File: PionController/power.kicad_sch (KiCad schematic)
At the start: 25 parts, among them U2 TPS562200, U3 TPS562200

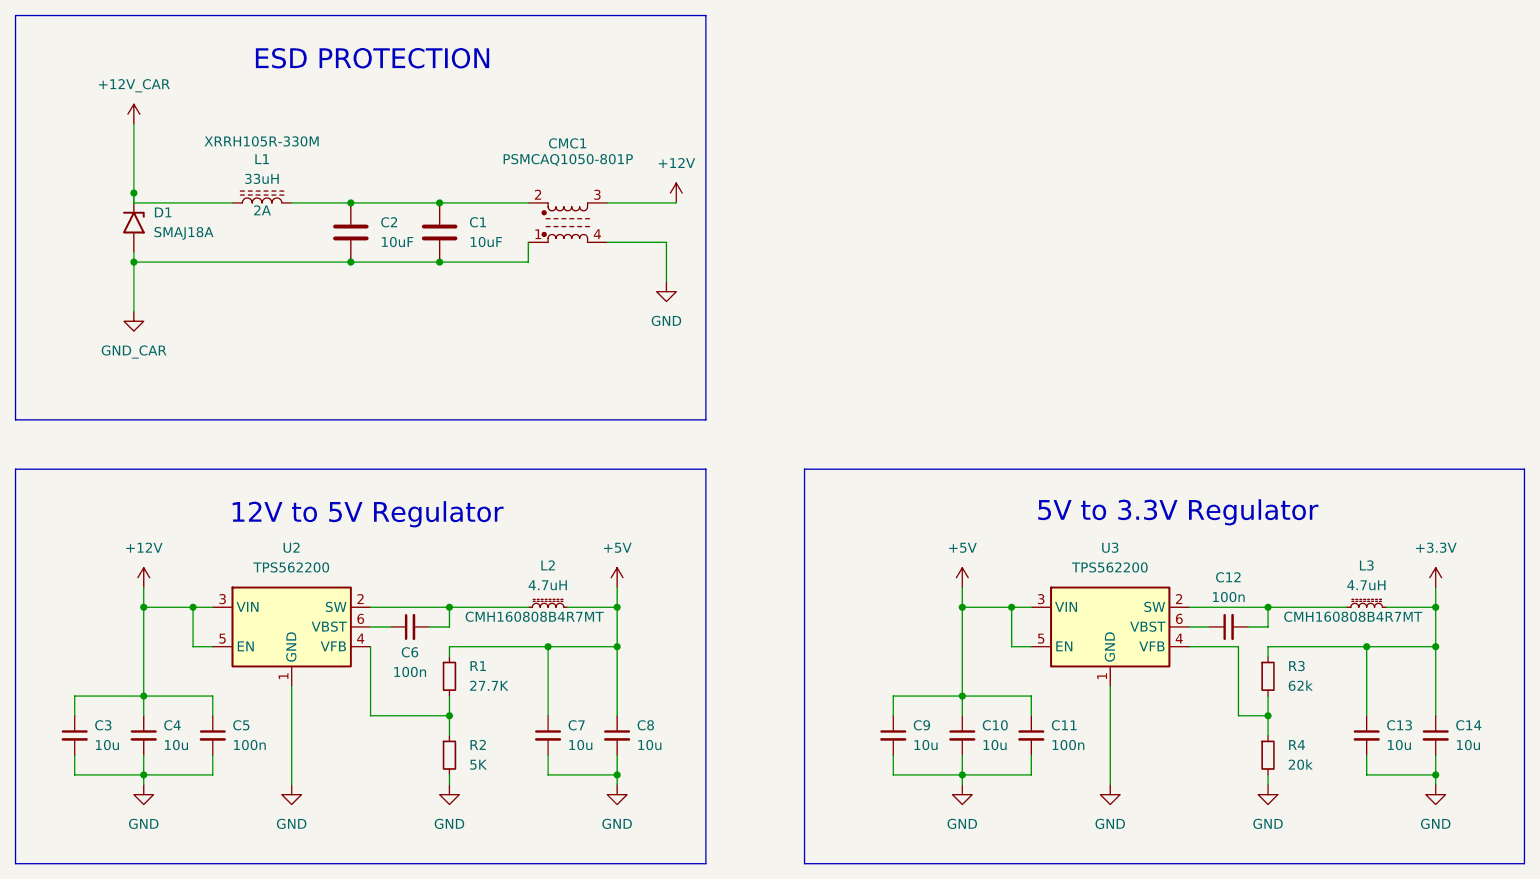
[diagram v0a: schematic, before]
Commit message: Fixing Ivan's remarks and adding the forgotten pull-down resistor
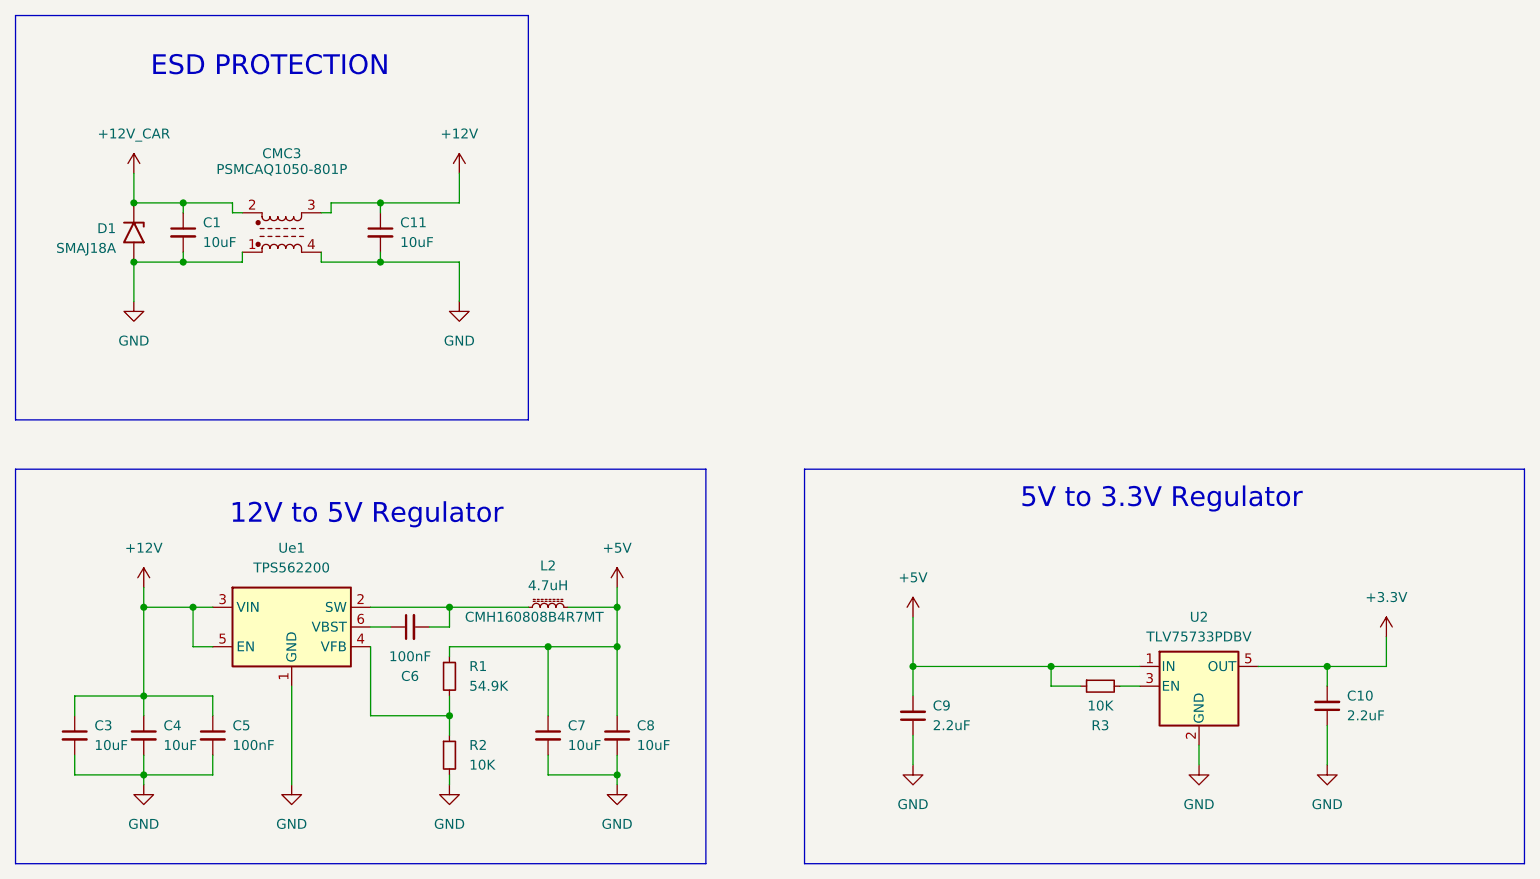
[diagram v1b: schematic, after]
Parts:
- removed C1, C2: 10uF, Capacitor_SMD:C_1210_3225Metric, symbol Device:C
- removed C12: 100n, Capacitor_SMD:C_0603_1608Metric, symbol Device:C_Small
- removed C13, C14: 10u, Capacitor_SMD:C_0603_1608Metric, symbol Device:C_Small
- removed L1: 33uH, Inductor_SMD:L_TDK_SLF10145, symbol Device:L_Ferrite
- removed L3: 4.7uH, Inductor_SMD:L_0603_1608Metric, symbol Device:L_Ferrite_Small
- removed R4: 20k, Resistor_SMD:R_0402_1005Metric, symbol Device:R_Small
- removed U3: TPS562200, Package_TO_SOT_SMD:SOT-23-6, symbol Regulator_Switching:TPS562200
- added C1: 10uF, Capacitor_SMD:C_1210_3225Metric, symbol Device:C_Small
- added U2: TLV75733PDBV, Package_TO_SOT_SMD:SOT-23-5, symbol Regulator_Linear:TLV75733PDBV
- C10, C9: value 10u -> 2.2uF; LCSC C7472961 -> C914769; MPN HGC0603R5106M250NTHJ -> (none); Manufacturer (none) -> CC0603KRX7R7BB225
- C11: value 100n -> 10uF; footprint Capacitor_SMD:C_0603_1608Metric -> Capacitor_SMD:C_1210_3225Metric; LCSC C6119861 -> C596319; MPN CGA0603X7R104K250JT -> (none); Manufacturer (none) -> CC1210KKX7R9BB106
- C3, C4, C7, C8: value 10u -> 10uF; footprint Capacitor_SMD:C_0603_1608Metric -> Capacitor_SMD:C_1210_3225Metric; LCSC C7472961 -> C596319; Manufacturer HGC0603R5106M250NTHJ -> CC1210KKX7R9BB106
- C5, C6: value 100n -> 100nF; footprint Capacitor_SMD:C_0603_1608Metric -> Capacitor_SMD:C_0805_2012Metric; LCSC C6119861 -> C111492; Manufacturer CGA0603X7R104K250JT -> CC0805JRX7R9BB104
- D1: LCSC (none) -> C148219; Manufacturer (none) -> SMAJ18A
- R1: value 27.7K -> 54.9K; footprint (none) -> Resistor_SMD:R_0805_2012Metric; LCSC C863005 -> C865555; Manufacturer RT0603DRE0727K7L -> RT0805BRD0754K9L
- R2: value 5K -> 10K; footprint (none) -> Resistor_SMD:R_0805_2012Metric; LCSC C870818 -> C110775; Manufacturer RT1206BRD075KL -> RT0805BRD0710KL
- R3: value 62k -> 10K; footprint Resistor_SMD:R_0402_1005Metric -> Resistor_SMD:R_0805_2012Metric; LCSC C37825 -> C84376; MPN 0402WGF6202TCE -> (none); Manufacturer (none) -> RC0805FR-0710KL
- renumbered CMC1 to CMC3, U2 to Ue1
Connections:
- net GND_CAR is gone; now on net GND: CMC3.1, D1.2 (A2)
- net +12V: now also C11.1
- net +12V_CAR: now also CMC3.2, C1.1
- net +3.3V: now also C10.2, U2.5 (OUT); no longer R3.1
- net +5V: now also C9.2, R3.1, U2.1 (IN); no longer C10.1, C11.1, C9.1
- net GND: now also C10.1, C9.1, C1.2, U2.2 (GND); no longer C10.2, C9.2
- net at R3.2: now also U2.3 (EN)
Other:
- moved on the sheet: CMC3, D1

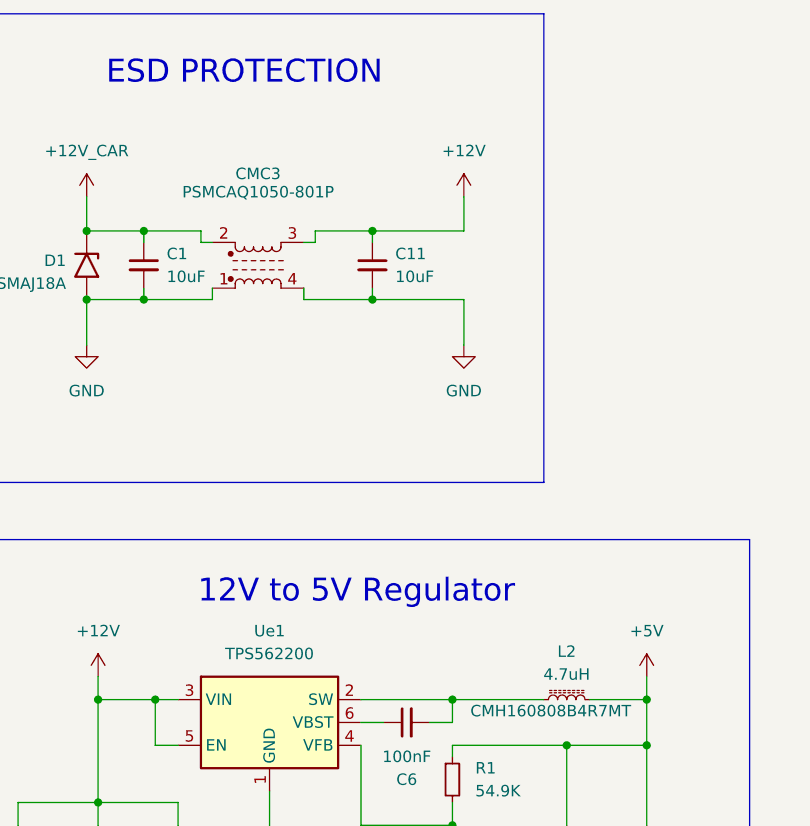
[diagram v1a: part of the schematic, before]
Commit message: Fixed reference designators in SCH and moved PCB silkscreen positions for better visibility
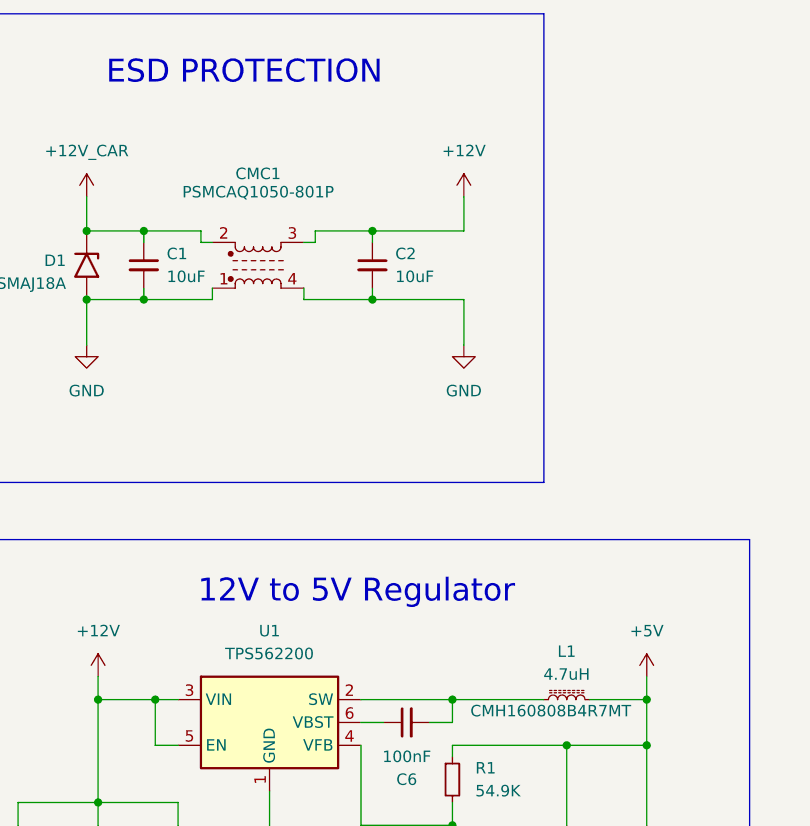
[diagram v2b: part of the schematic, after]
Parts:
- R3: Manufacturer RC0805FR-0710KL -> RC0805FR-0710KL
- renumbered C11 to C2, CMC3 to CMC1, L2 to L1, Ue1 to U1
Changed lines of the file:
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@@
+			)
+		)
+		(property "Package/Footprint" ""
+			(at 137.16 107.95 0)
+			(effects
+				(font
+					(size 1.27 1.27)
+				)
+				(hide yes)
 			)
 		)
@@
 			)
 		)
+		(property "Package/Footprint" ""
+			(at 43.18 45.72 0)
+			(effects
+				(font
+					(size 1.27 1.27)
+				)
+				(hide yes)
+			)
+		)
 		(pin "1"
 		)
@@
 			)
 		)
+		(property "Package/Footprint" ""
+			(at 77.47 102.87 0)
+			(effects
+				(font
+					(size 1.27 1.27)
+				)
+				(hide yes)
+			)
+		)
 		(pin "1"
 		)
@@
 		(dnp no)
 		(fields_autoplaced yes)
-		(property "Reference" "C11"
+		(property "Reference" "C2"
 			(at 71.12 44.4562 0)
 			(effects
@@
 			)
 		)
+		(property "Package/Footprint" ""
+			(at 68.58 45.72 0)
+			(effects
+				(font
+					(size 1.27 1.27)
+				)
+				(hide yes)
+			)
+		)
 		(pin "1"
 		)
@@
 			(project "PionController"
 				(path "/4c75befe-3f28-4e3b-aaa6-2731a1e568ad/9c944e10-f70f-4daf-a172-373cee634d1f"
-					(reference "C11")
+					(reference "C2")
 					(unit 1)
 				)
@@
 		(on_board yes)
 		(dnp no)
-		(property "Reference" "L2"
+		(property "Reference" "L1"
 			(at 90.17 88.646 90)
 			(effects
@@
 			)
 		)
+		(property "Package/Footprint" ""
+			(at 90.17 93.98 0)
+			(effects
+				(font
+					(size 1.27 1.27)
+				)
+				(hide yes)
+			)
+		)
 		(pin "1"
 		)
@@
 			(project "PionController"
 				(path "/4c75befe-3f28-4e3b-aaa6-2731a1e568ad/9c944e10-f70f-4daf-a172-373cee634d1f"
-					(reference "L2")
+					(reference "L1")
 					(unit 1)
 				)
@@
 			)
 		)
+		(property "Package/Footprint" ""
+			(at 38.1 110.49 0)
+			(effects
+				(font
+					(size 1.27 1.27)
+				)
+				(hide yes)
+			)
+		)
 		(pin "1"
 		)
@@
 			)
 		)
-		(property "Manufacturer" "  RC0805FR-0710KL"
+		(property "Manufacturer" "RC0805FR-0710KL"
 			(at 155.194 112.014 90)
 			(effects
@@
 					(size 1.27 1.27)
 				)
+			)
+		)
+		(property "Package/Footprint" ""
+			(at 161.29 104.14 0)
+			(effects
+				(font
+					(size 1.27 1.27)
+				)
+				(hide yes)
 			)
 		)
@@
 			)
 		)
+		(property "Package/Footprint" ""
+			(at 99.06 110.49 0)
+			(effects
+				(font
+					(size 1.27 1.27)
+				)
+				(hide yes)
+			)
+		)
 		(pin "1"
 		)
@@
 			)
 		)
+		(property "Package/Footprint" ""
+			(at 46.99 110.49 0)
+			(effects
+				(font
+					(size 1.27 1.27)
+				)
+				(hide yes)
+			)
+		)
 		(pin "1"
 		)
@@
 			)
 		)
+		(property "Package/Footprint" ""
+			(at 190.5 106.68 0)
+			(effects
+				(font
+					(size 1.27 1.27)
+				)
+				(hide yes)
+			)
+		)
 		(pin "1"
 		)
@@
 			)
 		)
+		(property "Package/Footprint" ""
+			(at 72.39 96.52 0)
+			(effects
+				(font
+					(size 1.27 1.27)
+				)
+				(hide yes)
+			)
+		)
 		(pin "1"
 		)
@@
 		(dnp no)
 		(fields_autoplaced yes)
-		(property "Reference" "Ue1"
+		(property "Reference" "U1"
 			(at 57.15 86.36 0)
 			(effects
@@
 			)
 		)
+		(property "Package/Footprint" ""
+			(at 57.15 96.52 0)
+			(effects
+				(font
+					(size 1.27 1.27)
+				)
+				(hide yes)
+			)
+		)
 		(pin "4"
 		)
@@
 			(project "PionController"
 				(path "/4c75befe-3f28-4e3b-aaa6-2731a1e568ad/9c944e10-f70f-4daf-a172-373cee634d1f"
-					(reference "Ue1")
+					(reference "U1")
 					(unit 1)
 				)
@@
 		(on_board yes)
 		(dnp no)
-		(property "Reference" "CMC3"
+		(property "Reference" "CMC1"
 			(at 55.88 35.56 0)
 			(effects
@@
 			)
 		)
+		(property "Package/Footprint" ""
+			(at 55.88 45.72 0)
+			(effects
+				(font
+					(size 1.27 1.27)
+				)
+				(hide yes)
+			)
+		)
 		(pin "1"
 		)
@@
 			(project "PionController"
 				(path "/4c75befe-3f28-4e3b-aaa6-2731a1e568ad/9c944e10-f70f-4daf-a172-373cee634d1f"
-					(reference "CMC3")
+					(reference "CMC1")
 					(unit 1)
 				)
@@
 			)
 		)
+		(property "Package/Footprint" ""
+			(at 90.17 110.49 0)
+			(effects
+				(font
+					(size 1.27 1.27)
+				)
+				(hide yes)
+			)
+		)
 		(pin "1"
 		)
@@
 			)
 		)
+		(property "Package/Footprint" ""
+			(at 77.47 113.03 0)
+			(effects
+				(font
+					(size 1.27 1.27)
+				)
+				(hide yes)
+			)
+		)
 		(pin "2"
 		)
@@
 			)
 		)
+		(property "Package/Footprint" ""
+			(at 29.21 110.49 0)
+			(effects
+				(font
+					(size 1.27 1.27)
+				)
+				(hide yes)
+			)
+		)
 		(pin "1"
 		)
@@
 		)
 		(property "Comment" ""
+			(at 36.83 45.72 0)
+			(effects
+				(font
+					(size 1.27 1.27)
+				)
+				(hide yes)
+			)
+		)
+		(property "Package/Footprint" ""
 			(at 36.83 45.72 0)
 			(effects
@@
 			(at 173.99 104.14 0)
 			(effects
+				(font
+					(size 1.27 1.27)
+				)
+				(hide yes)
+			)
+		)
+		(property "Package/Footprint" ""
+			(at 173.99 104.14 0)
+			(effects

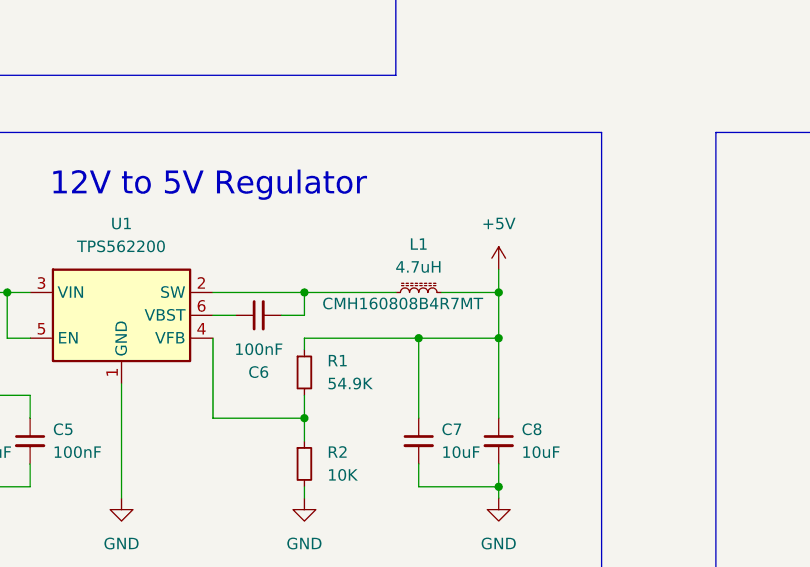
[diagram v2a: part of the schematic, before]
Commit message: New version 1.1
Fixing the inductor, the mixed up CPU the resistors, and the  f.silkscreen and b.silkscreen.
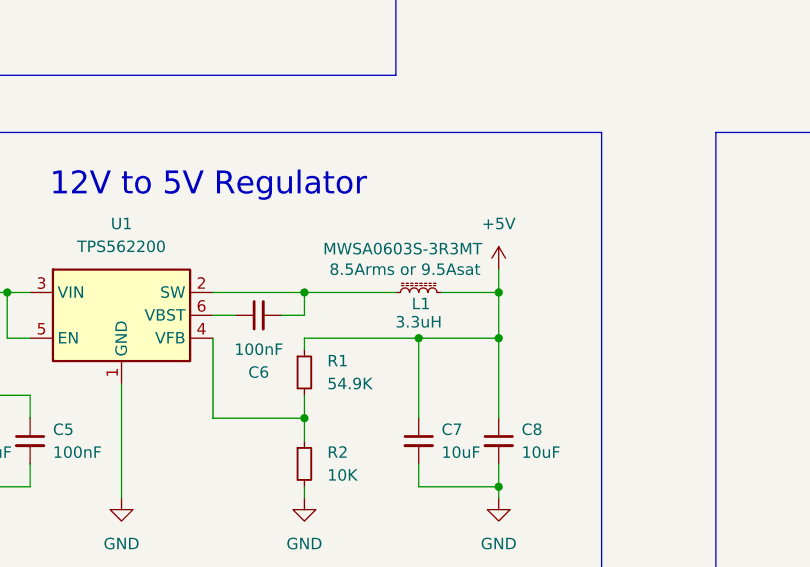
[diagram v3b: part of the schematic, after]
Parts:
- L1: value 4.7uH -> 3.3uH; footprint Inductor_SMD:L_0603_1608Metric -> Inductor_SMD:L_Sunlord_MWSA0603S; Comment Current min 0.5A -> Current >6.0A (22mR); Current 0.5A -> 8.5Arms or 9.5Asat; LCSC C394952 -> C408446; MPN (none) -> MWSA0603S-3R3MT; Manufacturer CMH160808B4R7MT -> (none); Model CMH160808B4R7MT -> MWSA0603S-3R3MT
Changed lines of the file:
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@@
-	)
-	(symbol
-		(lib_id "Device:L_Ferrite_Small")
-		(at 90.17 93.98 90)
-		(unit 1)
-		(exclude_from_sim no)
-		(in_bom yes)
-		(on_board yes)
-		(dnp no)
-		(property "Reference" "L1"
-			(at 90.17 88.646 90)
-			(effects
-				(font
-					(size 1.27 1.27)
-				)
-			)
-		)
-		(property "Value" "4.7uH"
-			(at 90.17 91.186 90)
-			(effects
-				(font
-					(size 1.27 1.27)
-				)
-			)
-		)
-		(property "Footprint" "Inductor_SMD:L_0603_1608Metric"
-			(at 90.17 93.98 0)
-			(effects
-				(font
-					(size 1.27 1.27)
-				)
-				(hide yes)
-			)
-		)
-		(property "Datasheet" "~"
-			(at 90.17 93.98 0)
-			(effects
-				(font
-					(size 1.27 1.27)
-				)
-				(hide yes)
-			)
-		)
-		(property "Description" "Inductor with ferrite core, small symbol"
-			(at 90.17 93.98 0)
-			(effects
-				(font
-					(size 1.27 1.27)
-				)
-				(hide yes)
-			)
-		)
-		(property "Model" "CMH160808B4R7MT"
-			(at 88.392 95.25 90)
-			(effects
-				(font
-					(size 1.27 1.27)
-				)
-			)
-		)
-		(property "LCSC" "C394952"
-			(at 90.17 93.98 90)
-			(effects
-				(font
-					(size 1.27 1.27)
-				)
-				(hide yes)
-			)
-		)
-		(property "Comment" "Current min 0.5A"
-			(at 90.17 93.98 0)
-			(effects
-				(font
-					(size 1.27 1.27)
-				)
-				(hide yes)
-			)
-		)
-		(property "Manufacturer" "CMH160808B4R7MT"
-			(at 90.17 93.98 0)
-			(effects
-				(font
-					(size 1.27 1.27)
-				)
-				(hide yes)
-			)
-		)
-		(property "Current" "0.5A"
-			(at 90.17 93.98 0)
-			(effects
-				(font
-					(size 1.27 1.27)
-				)
-				(hide yes)
-			)
-		)
-		(property "Package/Footprint" ""
-			(at 90.17 93.98 0)
-			(effects
-				(font
-					(size 1.27 1.27)
-				)
-				(hide yes)
-			)
-		)
-		(pin "1"
-		)
-		(pin "2"
-		)
-		(instances
-			(project "PionController"
-				(path "/4c75befe-3f28-4e3b-aaa6-2731a1e568ad/9c944e10-f70f-4daf-a172-373cee634d1f"
-					(reference "L1")
-					(unit 1)
-				)
-			)
-		)
 	)
 	(symbol
@@
 					(unit 1)
 				)
+			)
+		)
+	)
+	(symbol
+		(lib_id "Device:L_Ferrite_Small")
+		(at 90.17 93.98 90)
+		(unit 1)
+		(exclude_from_sim no)
+		(in_bom yes)
+		(on_board yes)
+		(dnp no)
+		(property "Reference" "L1"
+			(at 90.424 95.25 90)
+			(effects
+				(font
+					(size 1.27 1.27)
+				)
+			)
+		)
+		(property "Value" "3.3uH"
+			(at 90.17 97.282 90)
+			(effects
+				(font
+					(size 1.27 1.27)
+				)
+			)
+		)
+		(property "Footprint" "Inductor_SMD:L_Sunlord_MWSA0603S"
+			(at 90.17 93.98 0)
+			(effects
+				(font
+					(size 1.27 1.27)
+				)
+				(hide yes)
+			)
+		)
+		(property "Datasheet" "~"
+			(at 90.17 93.98 0)
+			(effects
+				(font
+					(size 1.27 1.27)
+				)
+				(hide yes)
+			)
+		)
+		(property "Description" "Inductor with ferrite core, small symbol"
+			(at 90.17 93.98 0)
+			(effects
+				(font
+					(size 1.27 1.27)
+				)
+				(hide yes)
+			)
+		)
+		(property "Model" "MWSA0603S-3R3MT"
+			(at 88.392 89.154 90)
+			(effects
+				(font
+					(size 1.27 1.27)
+				)
+			)
+		)
+		(property "Current" "8.5Arms or 9.5Asat"
+			(at 88.646 91.44 90)
+			(effects
+				(font
+					(size 1.27 1.27)
+				)
+			)
+		)
+		(property "LCSC" "C408446"
+			(at 90.17 93.98 90)
+			(effects
+				(font
+					(size 1.27 1.27)
+				)
+				(hide yes)
+			)
+		)
+		(property "Comment" "Current >6.0A (22mR)"
+			(at 90.17 93.98 0)
+			(effects
+				(font
+					(size 1.27 1.27)
+				)
+				(hide yes)
+			)
+		)
+		(property "MPN" " MWSA0603S-3R3MT"
+			(at 90.17 93.98 0)
+			(effects
+				(font
+					(size 1.27 1.27)
+				)
+				(hide yes)
+			)
+		)
+		(pin "1"
+		)
+		(pin "2"
+		)
+		(instances
+			(project "PionController"
+				(path "/4c75befe-3f28-4e3b-aaa6-2731a1e568ad/9c944e10-f70f-4daf-a172-373cee634d1f"
+					(reference "L1")
+					(unit 1)
+				)
